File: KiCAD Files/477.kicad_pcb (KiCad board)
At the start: 2 copper layers, 74 parts, among them IC1 W25N01GVSFIG, IC2 W25N01GVSFIG, IC3 W25N01GVSFIG, IC4 W25N01GVSFIG, IC5 AZ1117IH-3.3TRG1, IC6 USBLC6-2SC6, J1 BM06B-SRSS-TBT_LF__SN_, J2 6364372-2, J3 TSW-103-14-S-D, J4 TSW-103-14-S-D, J5 BM07B-SRSS-TB_LF__SN_, J6 BM09B-SRSS-TB_LF__SN_, U1 STM32H7A3RGTx, Y1 ABM8G-48.000MHZ-18-D2Y-T

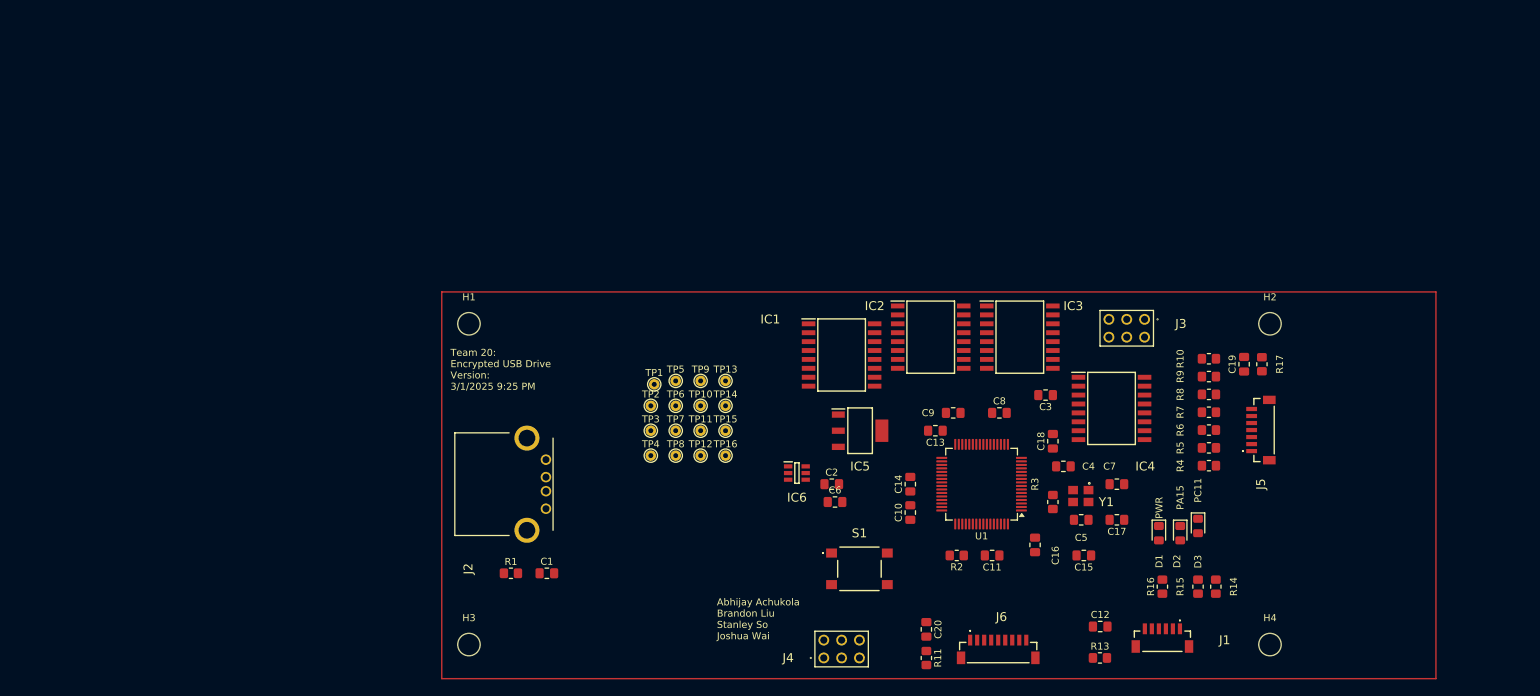
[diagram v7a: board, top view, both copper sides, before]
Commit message: routed essential signals
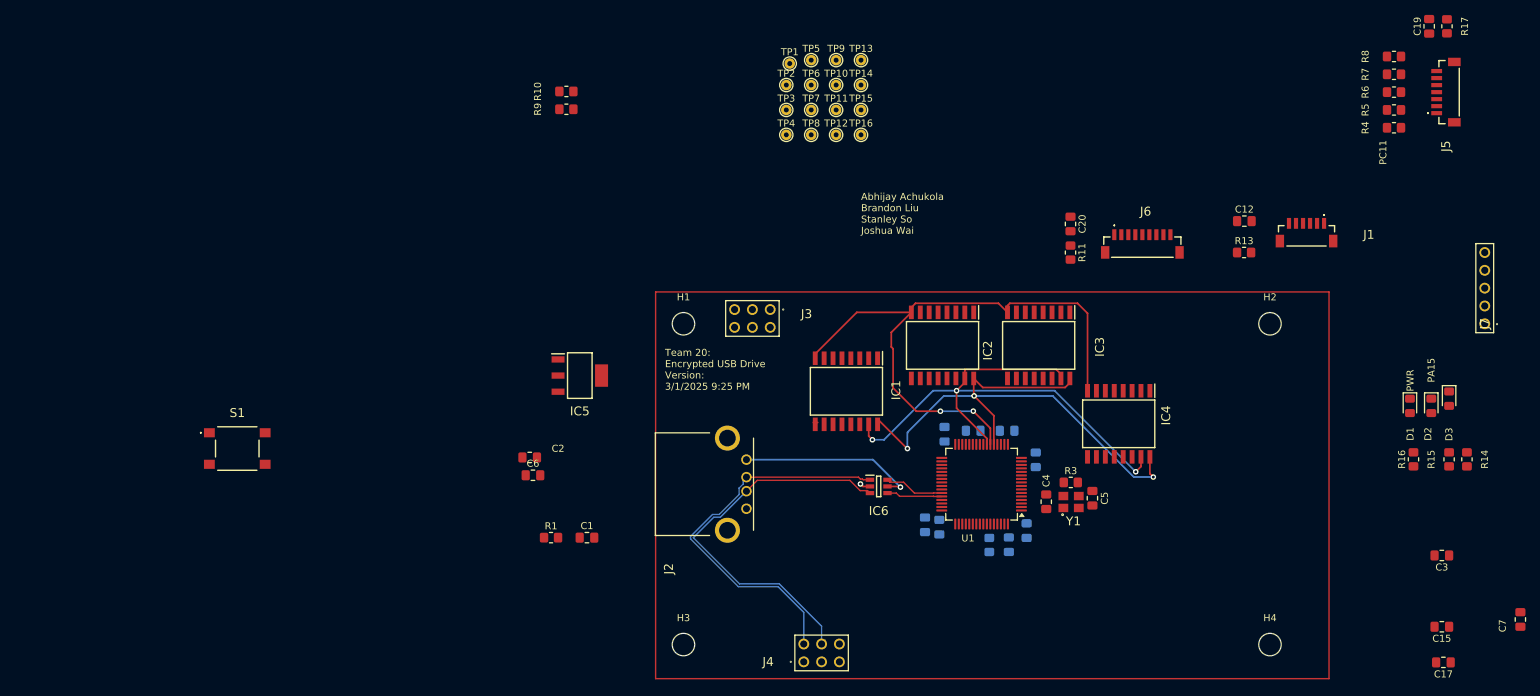
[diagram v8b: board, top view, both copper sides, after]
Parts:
- added J7: TSW-105-05-F-S, CustomFootprints:TSW-105-XX-YY-S, F.Cu at (259.1, 83.8)
- C10, C11, C13, C14, C16, C18, C8, C9, R2: moved to B.Cu
- moved R10 99.2 mm to (128.2, 50.7)
- moved R9 99.2 mm to (128.2, 53.2)
- moved S1 90.3 mm to (81.3, 101.6)
- moved J1 61.3 mm to (233.7, 71.1)
- moved J6 61.3 mm to (210.3, 72.9)
- moved R11 61.3 mm to (200.0, 73.7)
- moved C12 61.3 mm to (224.8, 69.2)
- moved C20 61.3 mm to (200.0, 69.6)
- moved R13 61.3 mm to (224.8, 73.7)
- moved C3 60.9 mm to (253.0, 116.8)
- moved C7 60.7 mm to (264.2, 126.0), turned to -90 degrees
- moved C19 54.9 mm to (251.2, 41.4)
- moved J5 54.9 mm to (254.0, 50.8)
- moved R17 54.9 mm to (253.7, 41.4)
- moved R6 54.9 mm to (246.1, 50.8)
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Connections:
- IC6 pad 4: PA12/USB+ -> USB+
- IC6 pad 6: PA11/USB- -> USB-
- J4 pad 2: GND -> D-
- J4 pad 4: PA11/USB- -> D+
- J4 pad 6: PA12/USB+ -> GND
- U1 pad 43: PA11/USB- -> USB-
- U1 pad 44: PA12/USB+ -> USB+
- U1 pad 45: PA13/JTMS/SWDIO -> PA13/SWDIO
- U1 pad 49: PA14/JTCK/SWCLK -> PA14/SWCLK
- U1 pad 50: PA14/JTCK/SWCLK -> unconnected-(U1-PA15-Pad50)
- U1 pad 55: PB3/JTDO -> unconnected-(U1-PB3-Pad55)
- U1 pad 56: PB4/nJTRST -> unconnected-(U1-PB4-Pad56)
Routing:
- net PA6/MISO: track 0.00 -> 86.7 mm, vias 0 -> 2
- net PA5/SCK: track 0.00 -> 79.4 mm, vias 0 -> 3
- net PA7/MOSI: track 0.00 -> 78.2 mm, vias 0 -> 3
- net D+: track 0.00 -> 56.3 mm
- net D-: track 0.00 -> 55.4 mm
- net +5V: track 0.00 -> 25.5 mm, vias 0 -> 1
- net USB-: track 0.00 -> 8.54 mm
- net USB+: track 0.00 -> 7.94 mm
- net GND: track 0.00 -> 1.49 mm, vias 0 -> 1
- net PC2/WP1: track 0.00 -> 0.62 mm
